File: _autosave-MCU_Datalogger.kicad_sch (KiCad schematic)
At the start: 25 parts, among them U1 24LC1025, U2 DS1337S_, U3 24LC1025, U4 ATMEGA328P-AU, Y1 32.768 KHz, Y2 16 MHz

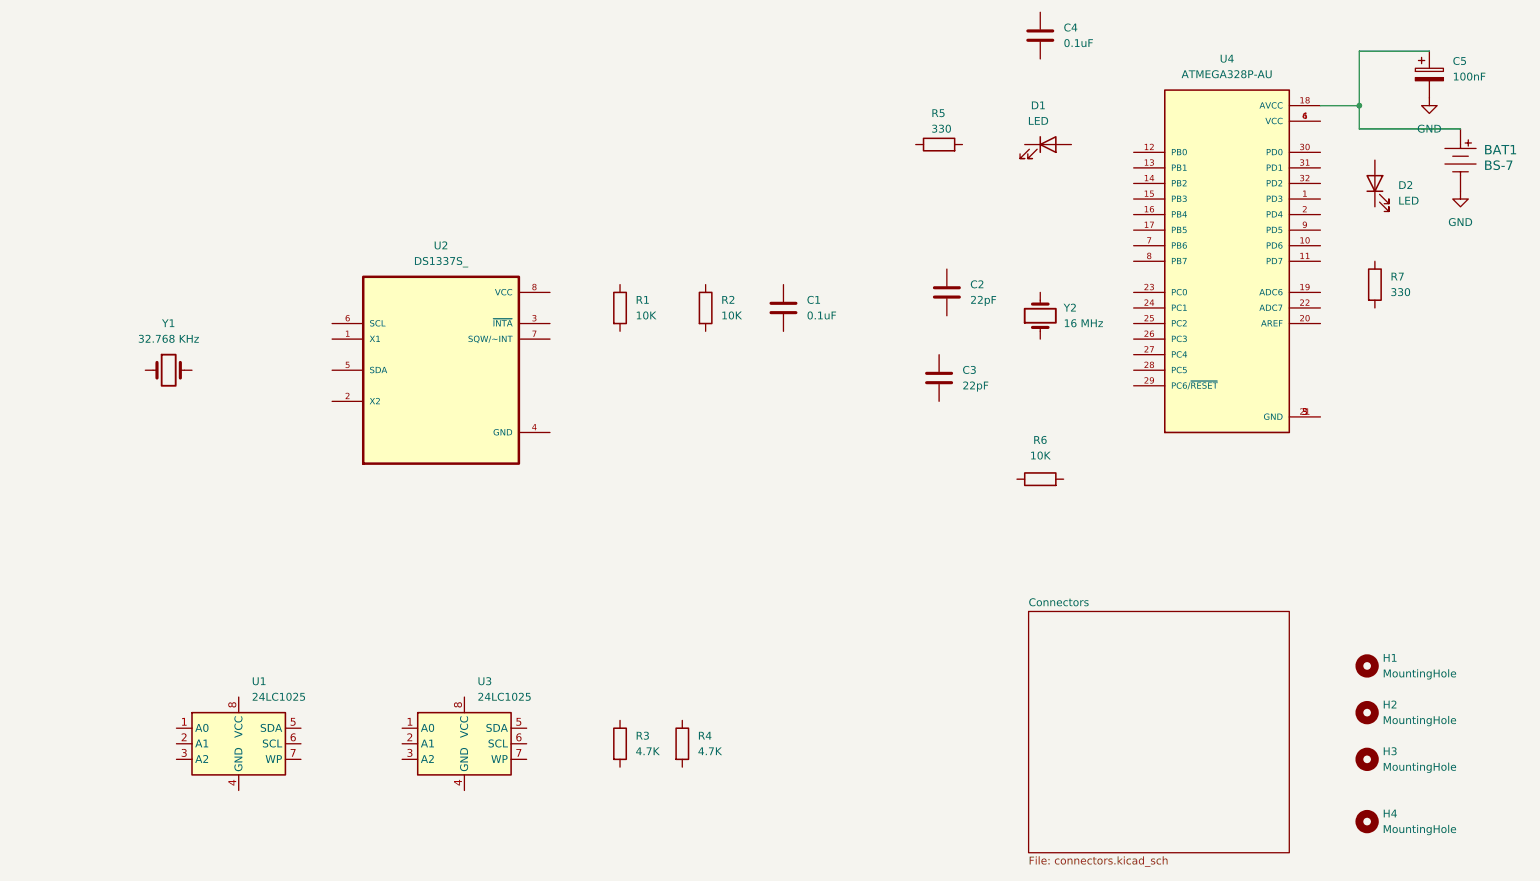
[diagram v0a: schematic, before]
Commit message: Completed wiring of main sheet.
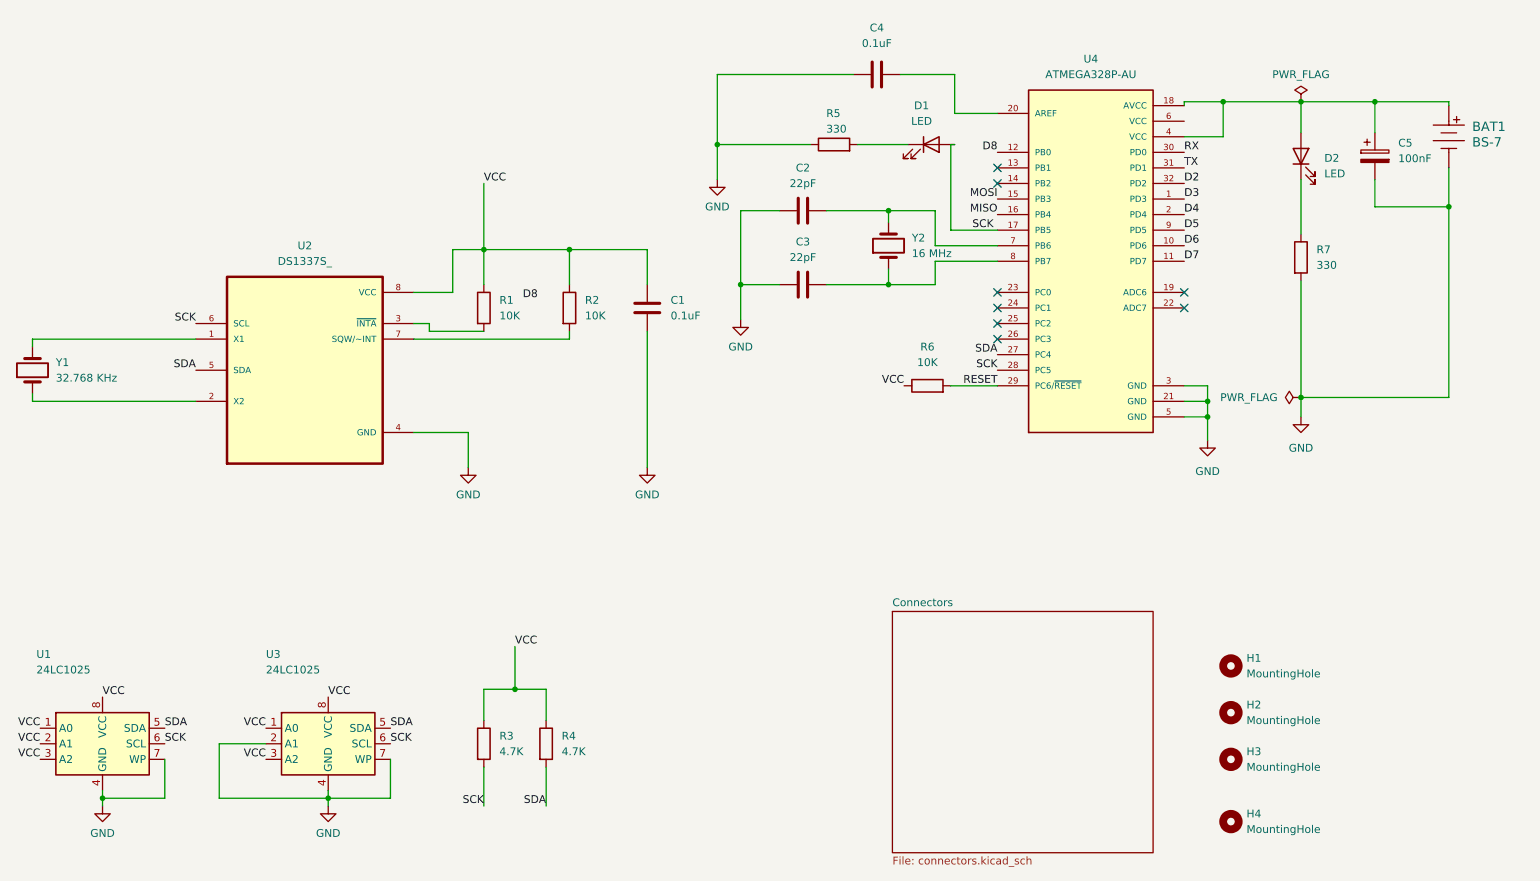
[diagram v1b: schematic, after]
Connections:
- net GND: now also C1.2, C2.1, C3.1, C4.1, R5.1, R7.2, U1.4 (GND), U1.7 (WP), U2.4 (GND), U3.2 (A1), U3.4 (GND), U3.7 (WP), U4.21 (GND), U4.3 (GND), U4.5 (GND)
- net VCC: now reaches R6.1
- net VCC: now also C1.1, R1.1, R2.1, R3.1, R4.1, U1.1 (A0), U1.2 (A1), U1.3 (A2), U1.8 (VCC), U2.8 (VCC), U3.1 (A0), U3.3 (A2), U3.8 (VCC)
- net RESET: now reaches R6.2
- net RESET: now also U4.29 (PC6/~{RESET})
- net at R1.2: now also U2.3 (~{INTA})
- net at Y1.1: now also U2.2 (X2)
- net at Y1.2: now also U2.1 (X1)
- net at D1.1 (K): now also R5.2
- net SCK: now reaches D1.2 (A)
- net SCK: now also R3.2, U1.6 (SCL), U2.6 (SCL), U3.6 (SCL), U4.17 (PB5), U4.28 (PC5)
- net at C2.2: now also U4.7 (PB6), Y2.2
- net SDA: now reaches U1.5 (SDA)
- net SDA: now also R4.2, U2.5 (SDA), U3.5 (SDA), U4.27 (PC4)
- net at U2.7 (SQW/~INT): now also R2.2
- net at Y2.1: now also C3.2, U4.8 (PB7)
- net at D2.1 (K): now also R7.1
- net at D2.2 (A): now also BAT1.Pos, C5.1, U4.18 (AVCC), U4.4 (VCC)
- net D3: now reaches U4.1 (PD3)
- net D6: now reaches U4.10 (PD6)
- net D7: now reaches U4.11 (PD7)
- net D8: now reaches U4.12 (PB0)
- net MOSI: now reaches U4.15 (PB3)
- net MISO: now reaches U4.16 (PB4)
- net D4: now reaches U4.2 (PD4)
- net at U4.20 (AREF): now also C4.2
- net RX: now reaches U4.30 (PD0)
- net TX: now reaches U4.31 (PD1)
- net D2: now reaches U4.32 (PD2)
- net at U4.6 (VCC): no longer U4.4 (VCC)
- net D5: now reaches U4.9 (PD5)
- no-connect marks 0 -> 8
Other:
- moved on the sheet: BAT1, C1, C2, C3, C4, C5, D1, D2, H1, H2, H3, H4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

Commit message: Completed wiring in the second sheet.
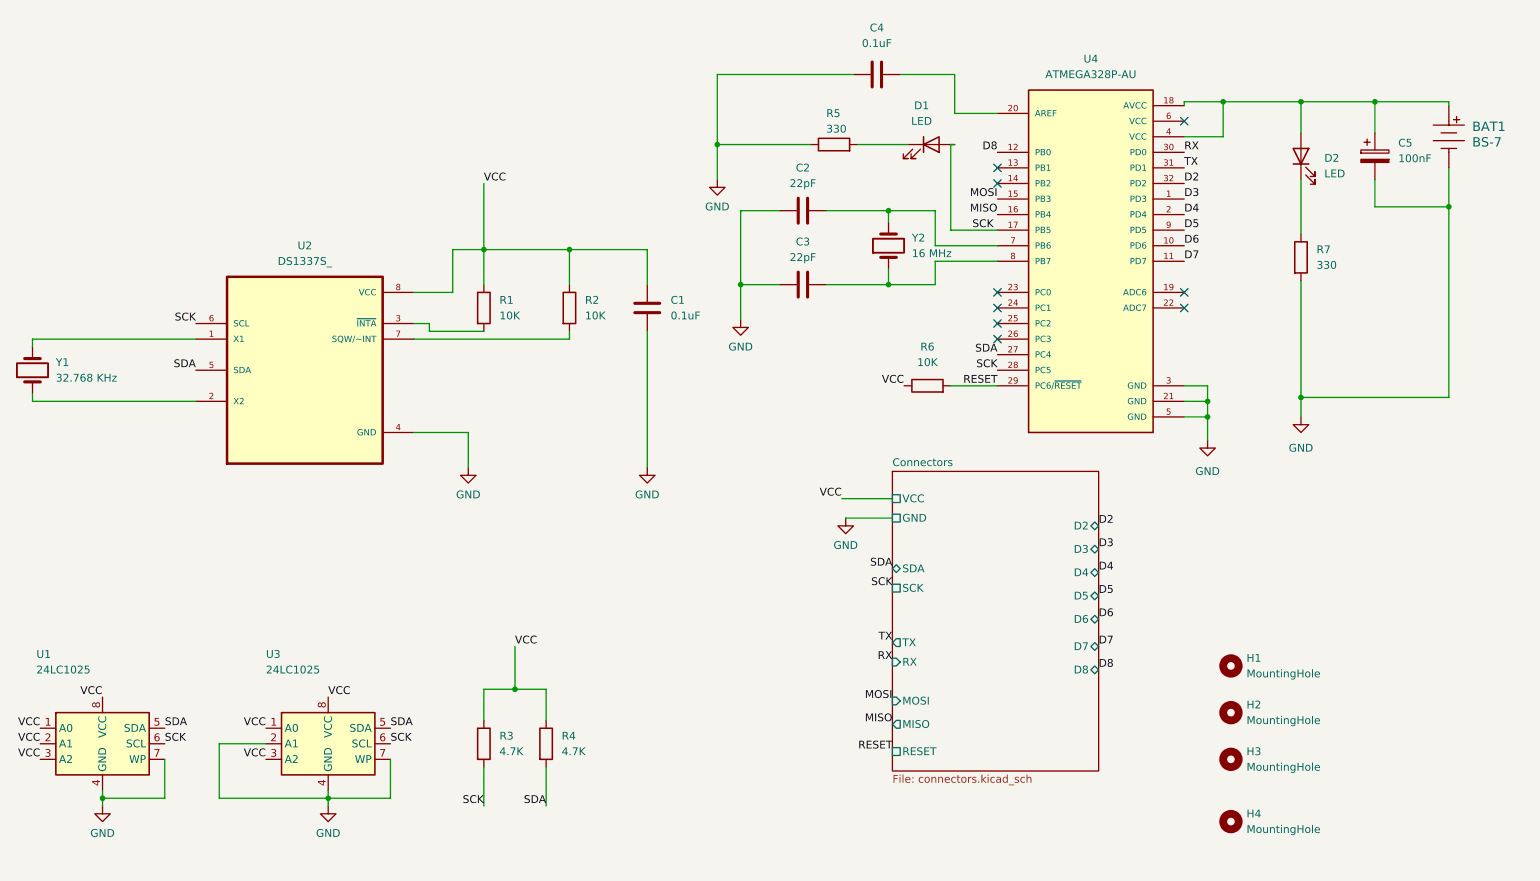
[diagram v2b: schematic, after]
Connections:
- no-connect marks 8 -> 9
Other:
- sheet Connectors ports: added D2, D3, D4, D5, D6, D7, D8, GND, MISO, MOSI, RESET, RX, SCK, SDA, TX, VCC; removed none

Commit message: Allocated GND and VCC nets to the Power net class.
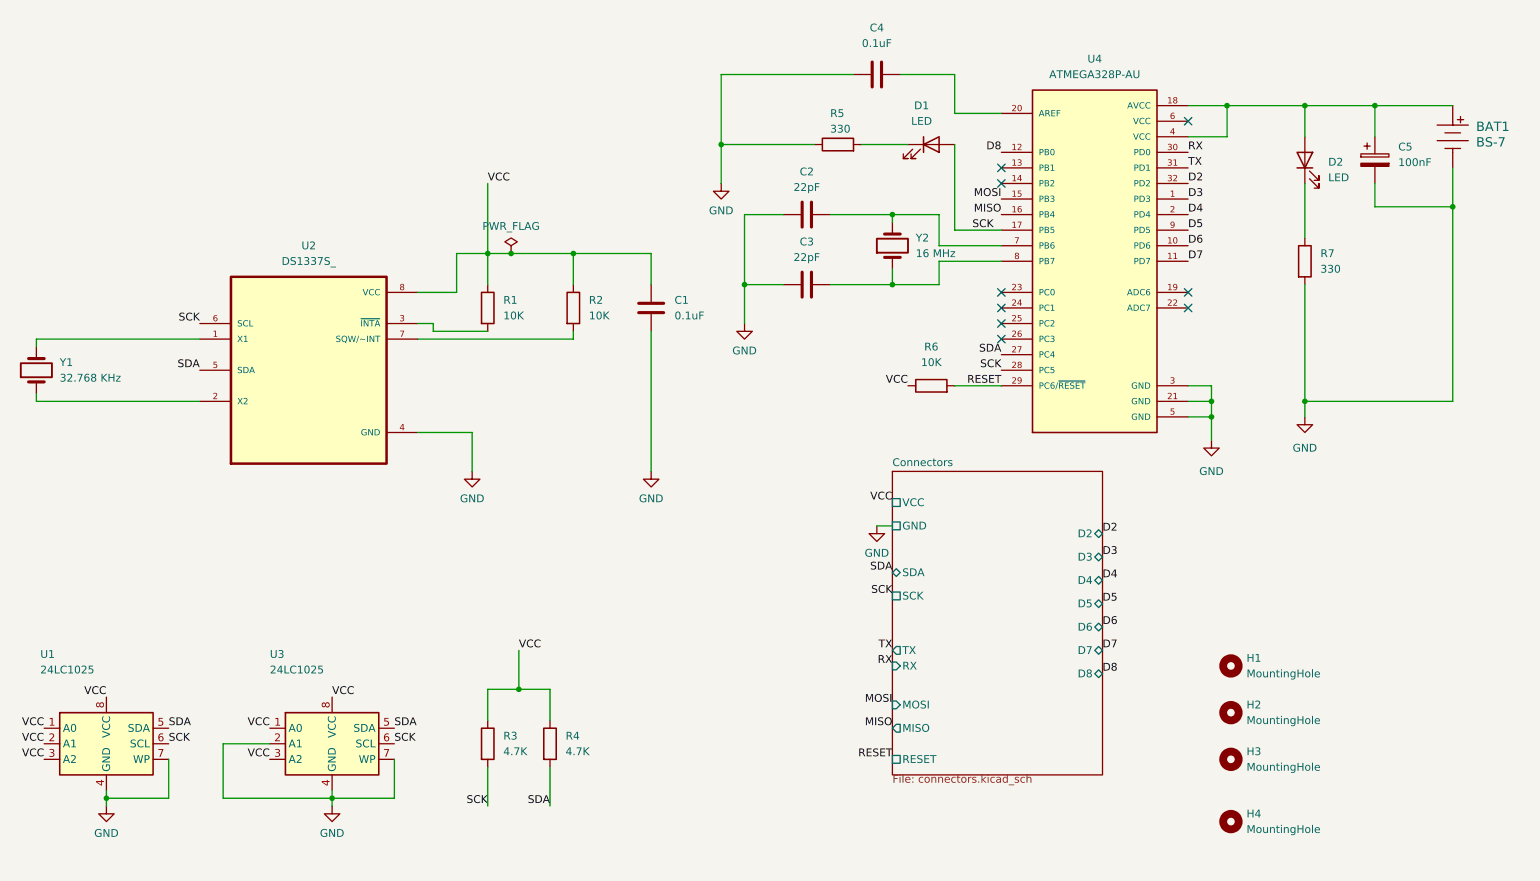
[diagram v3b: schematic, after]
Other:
- moved on the sheet: BAT1, C1, C2, C3, C5, D2, R1, R2, R3, R4, R5, R6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
